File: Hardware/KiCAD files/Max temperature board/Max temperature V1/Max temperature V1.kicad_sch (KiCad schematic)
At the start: 18 parts, among them J1 Conn_01x06, U13 MAX31865, X1 3.5mm, X2 3.5mm

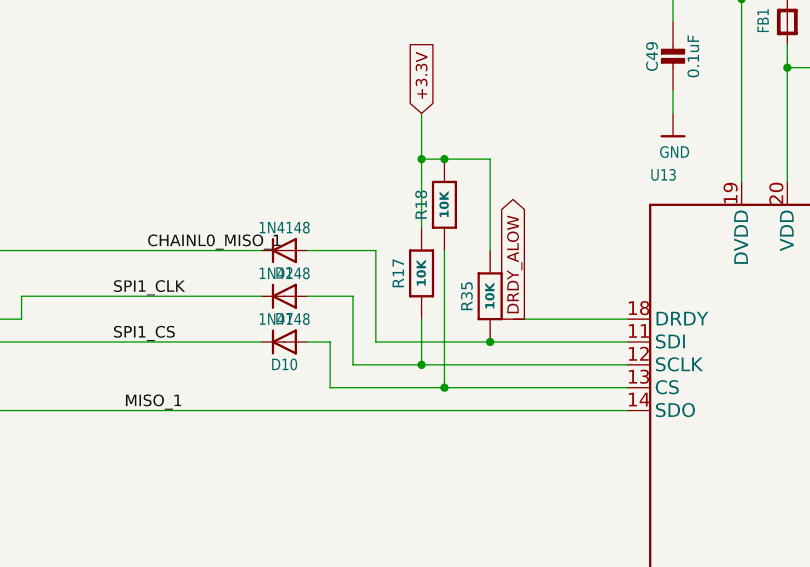
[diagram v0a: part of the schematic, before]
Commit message: 1st submitted iteration
added a folder for reviewing PCB's.
fixed various smaller issues on the PCB.
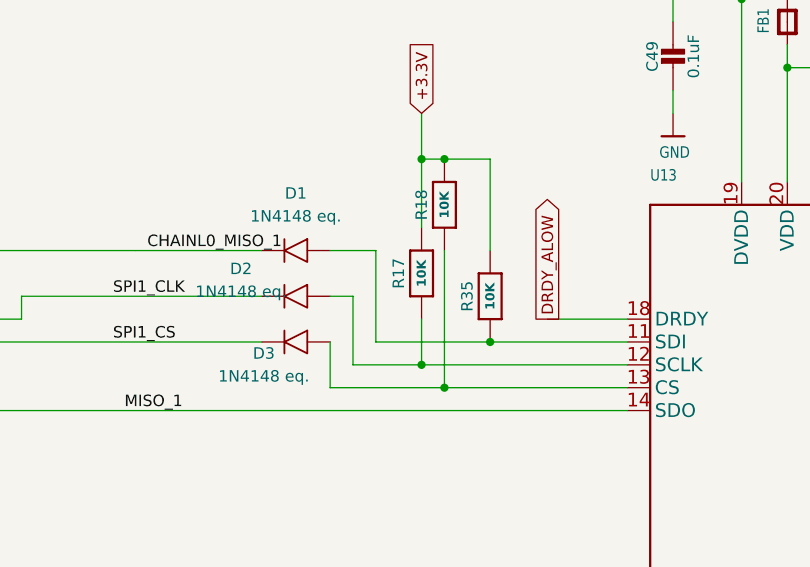
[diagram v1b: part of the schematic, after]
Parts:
- removed D10, D2, D7: 1N4148, Adafruit MAX31865:SOD-323, symbol Adafruit MAX31865-eagle-import:DIODESOD-323
- added D1, D2, D3: 1N4148 eq., Diode_THT:D_A-405_P10.16mm_Horizontal, symbol PCM_4ms_Diode:D_Generic
- C49, C50, C51: footprint Adafruit MAX31865:0805-NO -> Capacitor_SMD:C_0805_2012Metric
- FB1: footprint Adafruit MAX31865:0805-NO -> PCM_Ferrite_SMD_AKL:Ferrite_0805_2012Metric
- R17, R18, R35, R44: footprint Adafruit MAX31865:0805-NO -> Resistor_SMD:R_0805_2012Metric
- SJ1: footprint Adafruit MAX31865:SOLDERJUMPER_2WAY_OPEN_NOPASTE -> Jumper:SolderJumper-3_P1.3mm_Open_Pad1.0x1.5mm_NumberLabels
- SJ3, SJ4: footprint Adafruit MAX31865:SOLDERJUMPER_ARROW_NOPASTE -> Jumper:SolderJumper-2_P1.3mm_Open_Pad1.0x1.5mm
- U13: footprint Adafruit MAX31865:QFN20_4MM_0.65MM -> footprints:21-0056C_20_MXM
- X1, X2: footprint Adafruit MAX31865:TERMBLOCK_1X2-3.5MM -> TerminalBlock_4Ucon:TerminalBlock_4Ucon_1x02_P3.50mm_Horizontal
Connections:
- net CHAINL0_MISO_1: now also D1.1 (K)
- net SPI1_CLK: now also D2.1 (K)
- net SPI1_CS: now also D3.1 (K)
- net at R35.1, U13.11 (SDI): now also D1.2 (A)
- net at R18.1, U13.13 (CS): now also D3.2 (A)
- net at R17.1, U13.12 (SCLK): now also D2.2 (A)

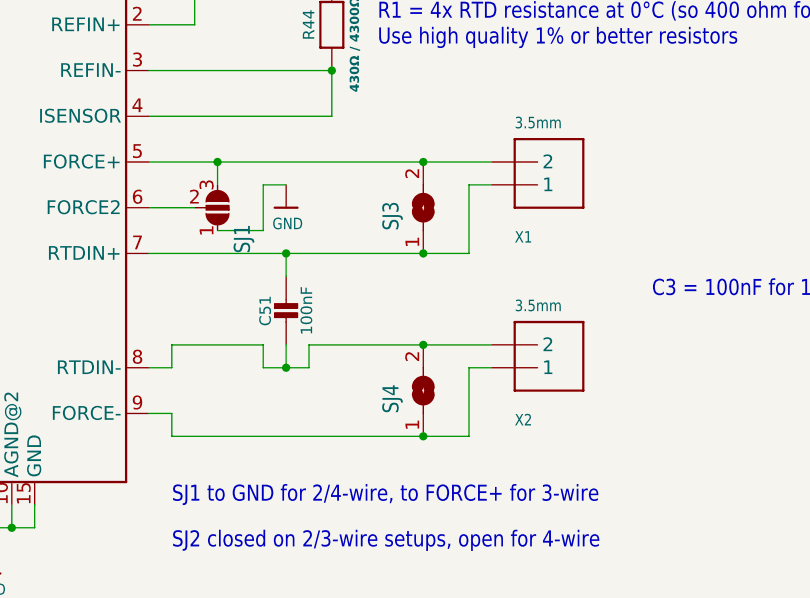
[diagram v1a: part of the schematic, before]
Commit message: Compatability mods
basic modifications to work toward compatability between boards physically on the hotend
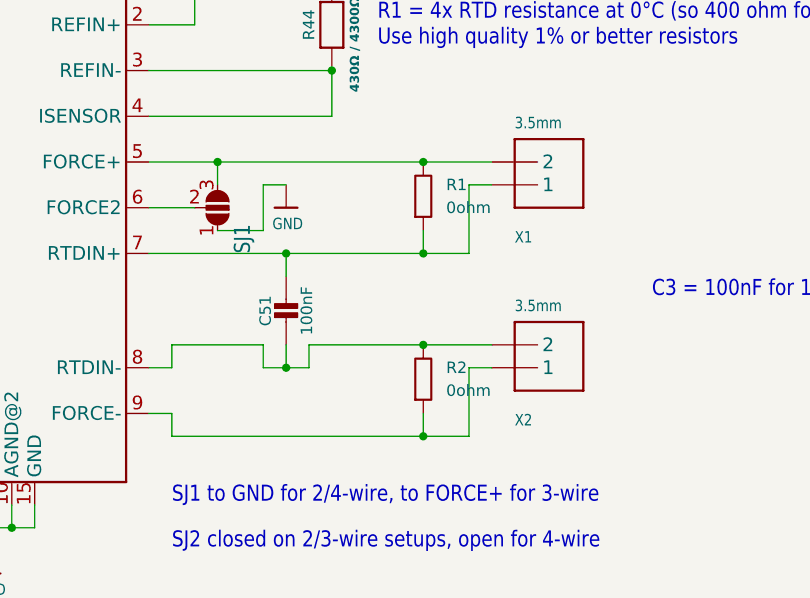
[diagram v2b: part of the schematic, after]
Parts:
- removed SJ3, SJ4: SOLDERJUMPER, Jumper:SolderJumper-2_P1.3mm_Open_Pad1.0x1.5mm, symbol Adafruit MAX31865-eagle-import:SOLDERJUMPER
- added R1, R2: 0ohm, Resistor_SMD:R_0805_2012Metric, symbol PCM_SL_Resistors:0ohm
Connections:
- net at C51.1, U13.7 (RTDIN+), X1.1: now also R1.1
- net at C51.2, U13.8 (RTDIN-), X2.2: now also R2.2
- net at U13.9 (FORCE-), X2.1: now also R2.1
- net at SJ1.3, U13.5 (FORCE+), X1.2: now also R1.2
